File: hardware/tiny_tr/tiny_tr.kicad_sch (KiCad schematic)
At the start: 24 parts, among them J1 Conn_01x02_Socket, SW1 SW_Push, SW2 SW_Push, SW3 SW_Push, SW4 SW_Push, U1 ATtiny85-20P, U2 PAM8302AAD, U3 ATtiny85-20P

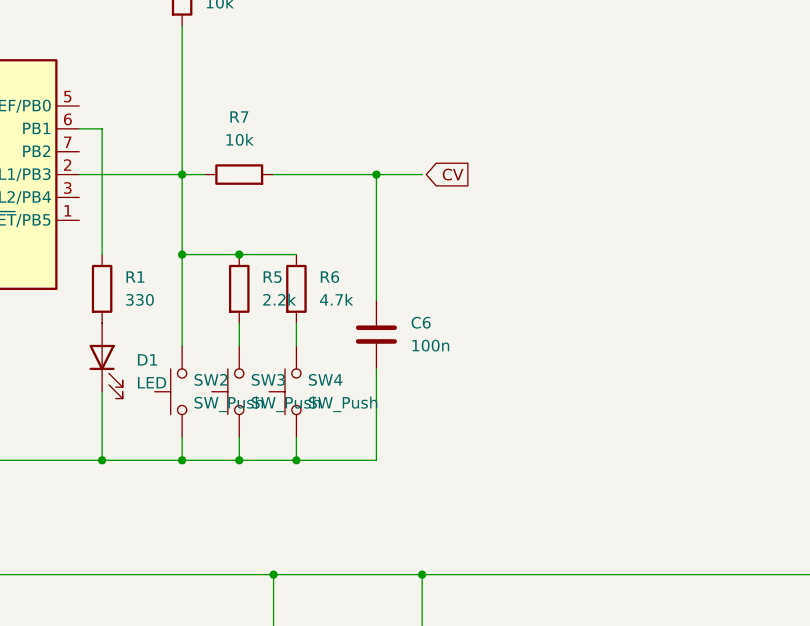
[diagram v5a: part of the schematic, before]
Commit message: fix(hardware): Add 10nF debounce capacitor to sequencer button input
Co-Authored-By: Claude Opus 4.5 <noreply@anthropic.com>
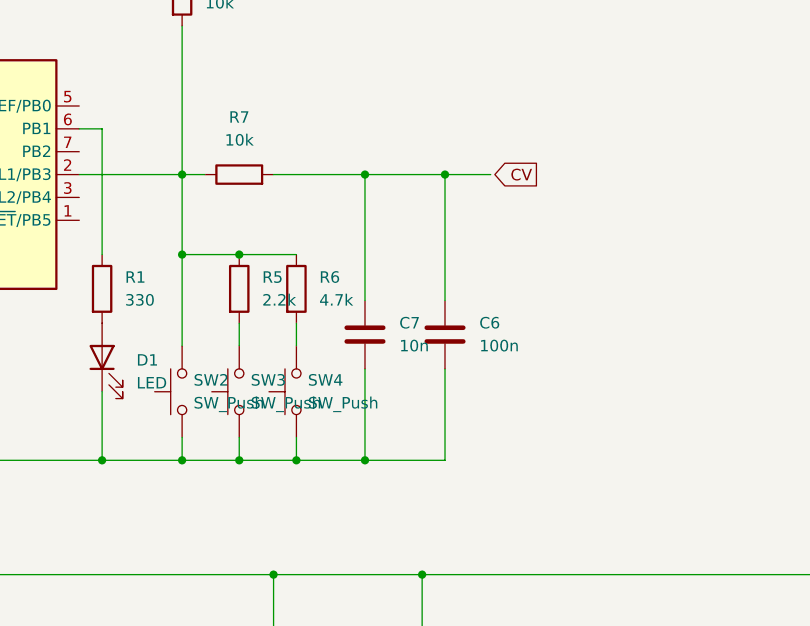
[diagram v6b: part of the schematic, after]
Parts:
- added C7: 10n, symbol Device:C
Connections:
- net GND: now also C7.2
- net at C6.1, R7.2: now also C7.1
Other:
- moved on the sheet: C6
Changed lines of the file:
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@@
+	)
+	(junction
+		(at 100.33 87.63)
+		(diameter 0)
+		(color 0 0 0 0)
 	)
 	(junction
@@
 	)
 	(junction
-		(at 101.6 55.88)
+		(at 109.22 55.88)
 		(diameter 0)
 		(color 0 0 0 0)
@@
 		(color 0 0 0 0)
 	)
+	(junction
+		(at 100.33 55.88)
+		(diameter 0)
+		(color 0 0 0 0)
+	)
 	(wire
 		(pts
@@
 	(wire
 		(pts
-			(xy 101.6 87.63) (xy 92.71 87.63)
+			(xy 109.22 87.63) (xy 100.33 87.63)
 		)
 		(stroke
@@
 	(wire
 		(pts
-			(xy 90.17 55.88) (xy 101.6 55.88)
+			(xy 90.17 55.88) (xy 100.33 55.88)
 		)
 		(stroke
@@
 	(wire
 		(pts
+			(xy 100.33 55.88) (xy 109.22 55.88)
+		)
+		(stroke
+			(width 0)
+			(type default)
+		)
+	)
+	(wire
+		(pts
 			(xy 173.99 160.02) (xy 185.42 160.02)
 		)
@@
 	(wire
 		(pts
+			(xy 100.33 77.47) (xy 100.33 87.63)
+		)
+		(stroke
+			(width 0)
+			(type default)
+		)
+	)
+	(wire
+		(pts
 			(xy 90.17 100.33) (xy 90.17 119.38)
 		)
@@
 	(wire
 		(pts
-			(xy 101.6 55.88) (xy 101.6 69.85)
+			(xy 109.22 55.88) (xy 109.22 69.85)
 		)
 		(stroke
@@
 	(wire
 		(pts
+			(xy 100.33 55.88) (xy 100.33 69.85)
+		)
+		(stroke
+			(width 0)
+			(type default)
+		)
+	)
+	(wire
+		(pts
 			(xy 53.34 27.94) (xy 80.01 27.94)
 		)
@@
 	(wire
 		(pts
+			(xy 100.33 87.63) (xy 92.71 87.63)
+		)
+		(stroke
+			(width 0)
+			(type default)
+		)
+	)
+	(wire
+		(pts
 			(xy 201.93 130.81) (xy 195.58 130.81)
 		)
@@
 	(wire
 		(pts
-			(xy 101.6 55.88) (xy 106.68 55.88)
-		)
-		(stroke
-			(width 0)
-			(type default)
-		)
-	)
-	(wire
-		(pts
-			(xy 101.6 77.47) (xy 101.6 87.63)
+			(xy 109.22 55.88) (xy 114.3 55.88)
+		)
+		(stroke
+			(width 0)
+			(type default)
+		)
+	)
+	(wire
+		(pts
+			(xy 109.22 77.47) (xy 109.22 87.63)
 		)
 		(stroke
@@
 	(global_label "CV"
 		(shape output)
-		(at 111.76 55.88 180)
+		(at 119.38 55.88 180)
 		(fields_autoplaced yes)
 		(effects
@@
 		)
 		(property "Intersheetrefs" "${INTERSHEET_REFS}"
-			(at 106.4162 55.88 0)
+			(at 114.0362 55.88 0)
 			(effects
 				(font
@@
 	(symbol
 		(lib_id "Device:C")
+		(at 100.33 73.66 0)
+		(unit 1)
+		(exclude_from_sim no)
+		(in_bom yes)
+		(on_board yes)
+		(dnp no)
+		(fields_autoplaced yes)
+		(property "Reference" "C7"
+			(at 104.14 72.3899 0)
+			(effects
+				(font
+					(size 1.27 1.27)
+				)
+				(justify left)
+			)
+		)
+		(property "Value" "10n"
+			(at 104.14 74.9299 0)
+			(effects
+				(font
+					(size 1.27 1.27)
+				)
+				(justify left)
+			)
+		)
+		(property "Footprint" ""
+			(at 101.2952 77.47 0)
+			(effects
+				(font
+					(size 1.27 1.27)
+				)
+				(hide yes)
+			)
+		)
+		(property "Datasheet" "~"
+			(at 100.33 73.66 0)
+			(effects
+				(font
+					(size 1.27 1.27)
+				)
+				(hide yes)
+			)
+		)
+		(property "Description" "Unpolarized capacitor"
+			(at 100.33 73.66 0)
+			(effects
+				(font
+					(size 1.27 1.27)
+				)
+				(hide yes)
+			)
+		)
+		(pin "2"
+		)
+		(pin "1"
+		)
+		(instances
+			(project ""
+				(path "/b0a62a77-cbdd-43ac-b9b7-6d13322499f8"
+					(reference "C7")
+					(unit 1)
+				)
+			)
+		)
+	)
+	(symbol
+		(lib_id "Device:C")
 		(at 173.99 148.59 0)
 		(unit 1)
@@
 	(symbol
 		(lib_id "Device:C")
-		(at 101.6 73.66 0)
+		(at 109.22 73.66 0)
 		(unit 1)
 		(exclude_from_sim no)
@@
 		(on_board yes)
 		(dnp no)
-		(fields_autoplaced yes)
 		(property "Reference" "C6"
-			(at 105.41 72.3899 0)
+			(at 113.03 72.3899 0)
 			(effects
 				(font
@@
 		)
 		(property "Value" "100n"
-			(at 105.41 74.9299 0)
+			(at 113.03 74.9299 0)
 			(effects
 				(font
@@
 		)
 		(property "Footprint" ""
-			(at 102.5652 77.47 0)
+			(at 110.1852 77.47 0)
 			(effects
 				(font
@@
 		)
 		(property "Datasheet" "~"
-			(at 101.6 73.66 0)
+			(at 109.22 73.66 0)
 			(effects
 				(font
@@
 		)
 		(property "Description" "Unpolarized capacitor"
-			(at 101.6 73.66 0)
-			(effects
-				(font
+			(at 109.22 73.66 0)
+			(effects
+				(font
